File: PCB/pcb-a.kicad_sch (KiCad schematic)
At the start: 20 parts, among them Q3 BC337, Q4 BC337, SW1 config, U1 MCP23008-xP, U4 ATmega16L-8P, Y1 8Mhz

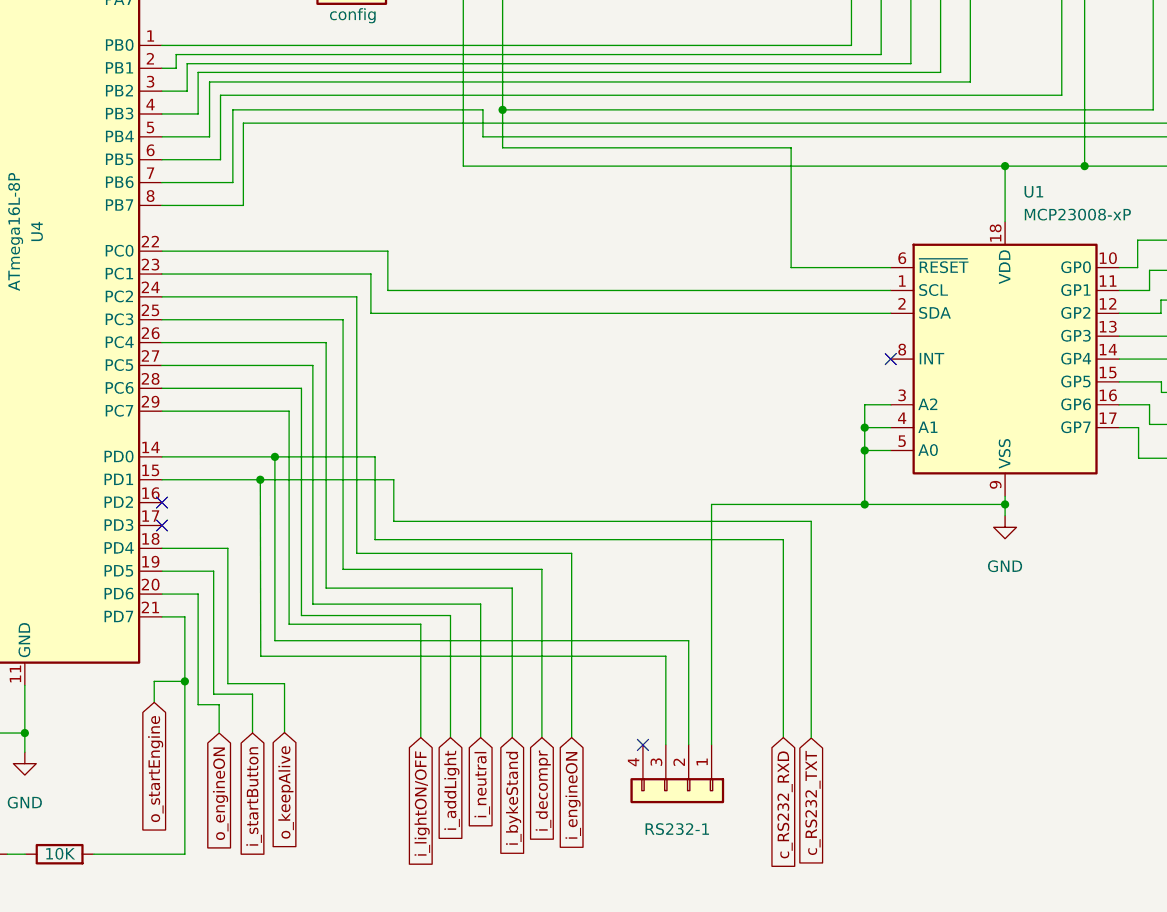
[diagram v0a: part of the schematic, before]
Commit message: Enhancement: RS232 port
RS232 4-wire connector is compatible with MAX232 driver module
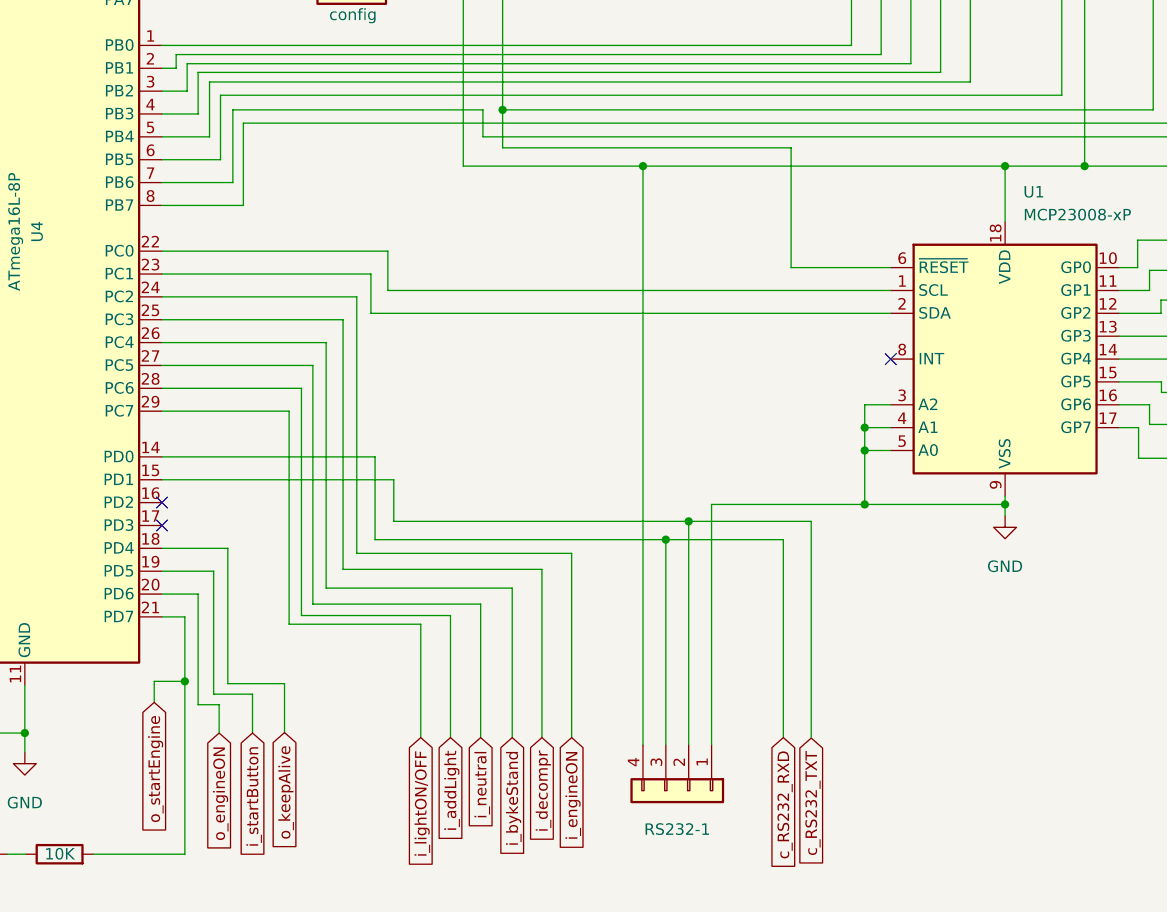
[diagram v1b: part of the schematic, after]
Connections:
- net c_RS232_RXD: now also RS232-1.3 (Pin_3); no longer RS232-1.2 (Pin_2)
- net c_RS232_TXT: now also RS232-1.2 (Pin_2); no longer RS232-1.3 (Pin_3)
- net tempPower: now also RS232-1.4 (Pin_4)
- no-connect marks 9 -> 8
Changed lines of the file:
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@@
   )
   (bus_alias "port-b" (members "PB0" "PB1" "PB2" "PB3" "PB4" "PB5" "PB6" "PB7"))
-  (junction (at 85.2424 121.158) (diameter 0) (color 0 0 0 0)
-  )
   (junction (at 59.0804 35.306) (diameter 0) (color 0 0 0 0)
   )
@@
   (junction (at 59.0804 149.3012) (diameter 0) (color 0 0 0 0)
   )
+  (junction (at 127.762 86.3092) (diameter 0) (color 0 0 0 0)
+  )
   (junction (at 40.8432 35.306) (diameter 0) (color 0 0 0 0)
   )
@@
   (junction (at 40.8432 45.8724) (diameter 0) (color 0 0 0 0)
   )
-  (junction (at 86.868 118.618) (diameter 0) (color 0 0 0 0)
-  )
   (junction (at 152.4 123.9012) (diameter 0) (color 0 0 0 0)
   )
@@
   (junction (at 176.8348 86.3092) (diameter 0) (color 0 0 0 0)
   )
+  (junction (at 130.302 127.8128) (diameter 0) (color 0 0 0 0)
+  )
   (junction (at 152.4 115.3668) (diameter 0) (color 0 0 0 0)
   )
@@
   )
   (junction (at 36.8808 62.738) (diameter 0) (color 0 0 0 0)
+  )
+  (junction (at 132.842 125.7808) (diameter 0) (color 0 0 0 0)
   )
   (junction (at 33.9852 86.8172) (diameter 0) (color 0 0 0 0)
@@
   (no_connect (at 74.3204 62.738))
   (no_connect (at 186.9948 49.4792))
-  (no_connect (at 127.762 150.622))
   (no_connect (at 61.6204 42.418))
   (no_connect (at 74.3204 60.198))
@@
     (stroke (width 0) (type default) (color 0 0 0 0))
   )
-  (wire (pts (xy 74.3204 118.618) (xy 86.868 118.618))
+  (wire (pts (xy 74.3204 118.618) (xy 97.9932 118.618))
     (stroke (width 0) (type default) (color 0 0 0 0))
   )
@@
     (stroke (width 0) (type default) (color 0 0 0 0))
   )
-  (wire (pts (xy 132.842 139.0396) (xy 86.868 139.0396))
-    (stroke (width 0) (type default) (color 0 0 0 0))
-  )
   (wire (pts (xy 74.3204 52.578) (xy 93.1164 52.578))
     (stroke (width 0) (type default) (color 0 0 0 0))
   )
+  (wire (pts (xy 127.762 86.3092) (xy 107.7976 86.3092))
+    (stroke (width 0) (type default) (color 0 0 0 0))
+  )
   (wire (pts (xy 74.3204 95.758) (xy 99.4156 95.758))
     (stroke (width 0) (type default) (color 0 0 0 0))
@@
     (stroke (width 0) (type default) (color 0 0 0 0))
   )
-  (wire (pts (xy 130.302 140.7668) (xy 130.302 150.622))
+  (wire (pts (xy 130.302 127.8128) (xy 130.302 150.622))
     (stroke (width 0) (type default) (color 0 0 0 0))
   )
@@
     (stroke (width 0) (type default) (color 0 0 0 0))
   )
-  (wire (pts (xy 97.9932 127.8128) (xy 143.3576 127.8128))
+  (wire (pts (xy 97.9932 127.8128) (xy 130.302 127.8128))
     (stroke (width 0) (type default) (color 0 0 0 0))
   )
@@
     (stroke (width 0) (type default) (color 0 0 0 0))
   )
-  (wire (pts (xy 132.842 139.0396) (xy 132.842 150.622))
+  (wire (pts (xy 132.842 125.7808) (xy 132.842 150.622))
     (stroke (width 0) (type default) (color 0 0 0 0))
   )
@@
     (stroke (width 0) (type default) (color 0 0 0 0))
   )
+  (wire (pts (xy 132.842 125.7808) (xy 146.4564 125.7808))
+    (stroke (width 0) (type default) (color 0 0 0 0))
+  )
   (wire (pts (xy 184.0484 115.0112) (xy 184.0484 112.8268))
     (stroke (width 0) (type default) (color 0 0 0 0))
@@
     (stroke (width 0) (type default) (color 0 0 0 0))
   )
-  (wire (pts (xy 100.076 125.7808) (xy 146.4564 125.7808))
+  (wire (pts (xy 100.076 125.7808) (xy 132.842 125.7808))
     (stroke (width 0) (type default) (color 0 0 0 0))
   )
@@
     (stroke (width 0) (type default) (color 0 0 0 0))
   )
-  (wire (pts (xy 74.3204 121.158) (xy 85.2424 121.158))
-    (stroke (width 0) (type default) (color 0 0 0 0))
-  )
-  (wire (pts (xy 85.2932 140.7668) (xy 130.302 140.7668))
-    (stroke (width 0) (type default) (color 0 0 0 0))
-  )
   (wire (pts (xy 40.8432 50.038) (xy 43.8404 50.038))
     (stroke (width 0) (type default) (color 0 0 0 0))
   )
-  (wire (pts (xy 86.868 118.618) (xy 97.9932 118.618))
+  (wire (pts (xy 130.302 127.8128) (xy 143.3576 127.8128))
     (stroke (width 0) (type default) (color 0 0 0 0))
   )
@@
     (stroke (width 0) (type default) (color 0 0 0 0))
   )
-  (wire (pts (xy 85.2932 140.7668) (xy 85.2424 121.158))
-    (stroke (width 0) (type default) (color 0 0 0 0))
-  )
   (wire (pts (xy 152.4 123.9012) (xy 167.9956 123.9012))
     (stroke (width 0) (type default) (color 0 0 0 0))
@@
     (stroke (width 0) (type default) (color 0 0 0 0))
   )
+  (wire (pts (xy 127.762 86.3092) (xy 127.762 150.622))
+    (stroke (width 0) (type default) (color 0 0 0 0))
+  )
   (wire (pts (xy 155.2956 97.5868) (xy 144.2212 97.5868))
     (stroke (width 0) (type default) (color 0 0 0 0))
@@
     (stroke (width 0) (type default) (color 0 0 0 0))
   )
-  (wire (pts (xy 85.2424 121.158) (xy 100.076 121.158))
+  (wire (pts (xy 74.3204 121.158) (xy 100.076 121.158))
     (stroke (width 0) (type default) (color 0 0 0 0))
   )
@@
     (stroke (width 0) (type default) (color 0 0 0 0))
   )
-  (wire (pts (xy 167.9956 86.3092) (xy 107.7976 86.3092))
+  (wire (pts (xy 167.9956 86.3092) (xy 127.762 86.3092))
     (stroke (width 0) (type default) (color 0 0 0 0))
   )
@@
     (stroke (width 0) (type default) (color 0 0 0 0))
   )
-  (wire (pts (xy 86.868 118.618) (xy 86.868 139.0396))
-    (stroke (width 0) (type default) (color 0 0 0 0))
-  )

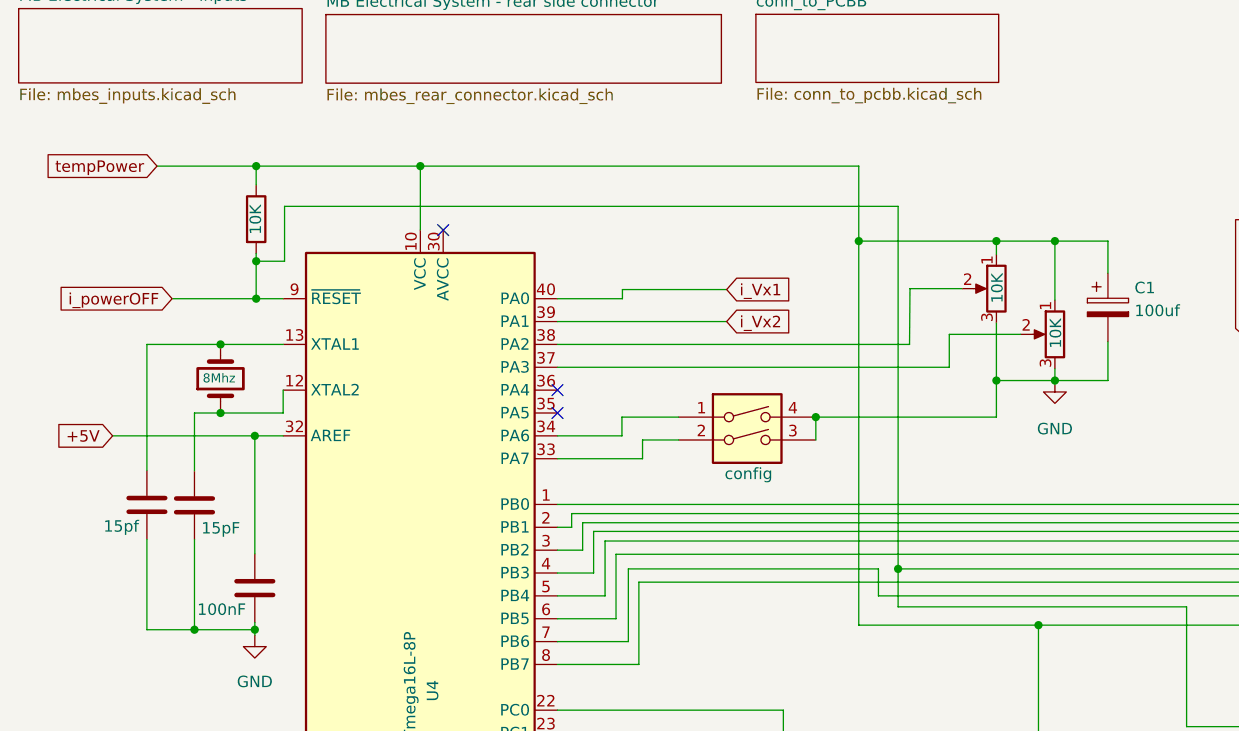
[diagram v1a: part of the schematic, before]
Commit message: Fixes for analog inputs
- ground reference missed
- AVCC was not connected
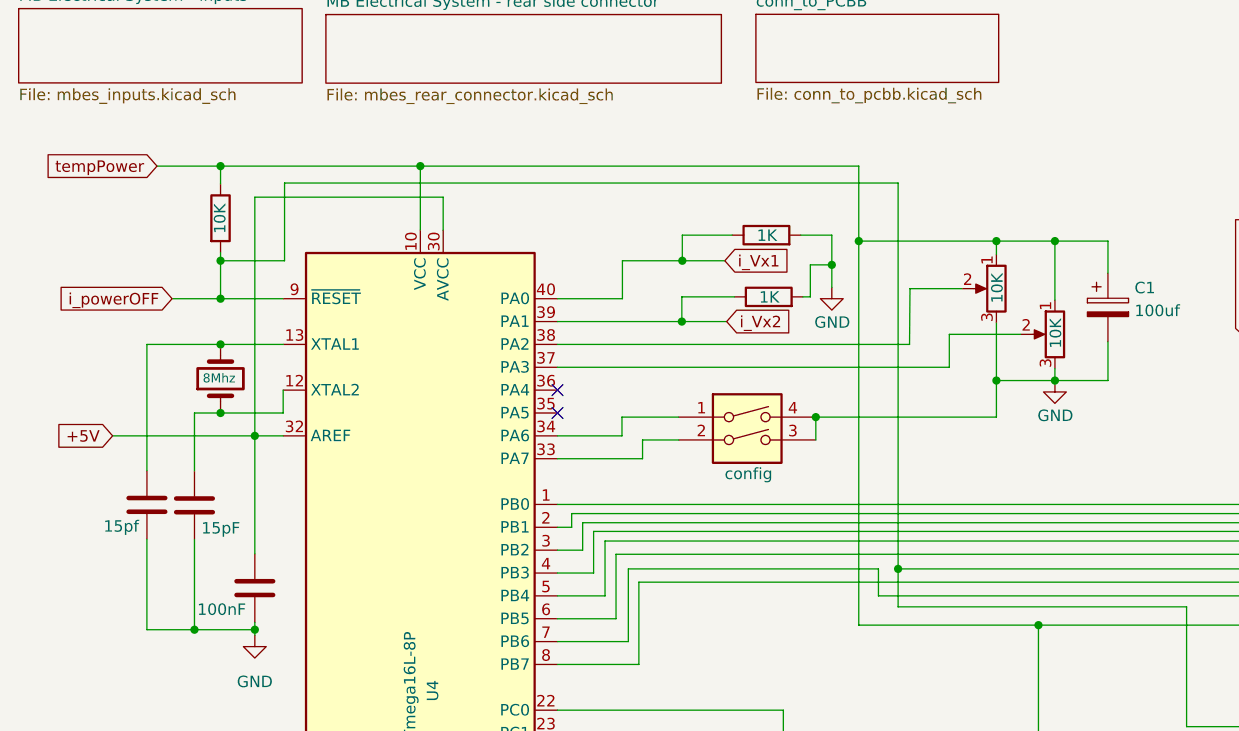
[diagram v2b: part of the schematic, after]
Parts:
- added R3, R4: 1K, Resistor_THT:R_Axial_DIN0207_L6.3mm_D2.5mm_P7.62mm_Horizontal, symbol Device:R
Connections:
- net +5V: now also U4.30 (AVCC)
- net GND: now also R3.2, R4.2
- net i_Vx1: now also R3.1
- net i_Vx2: now also R4.1
- no-connect marks 8 -> 7

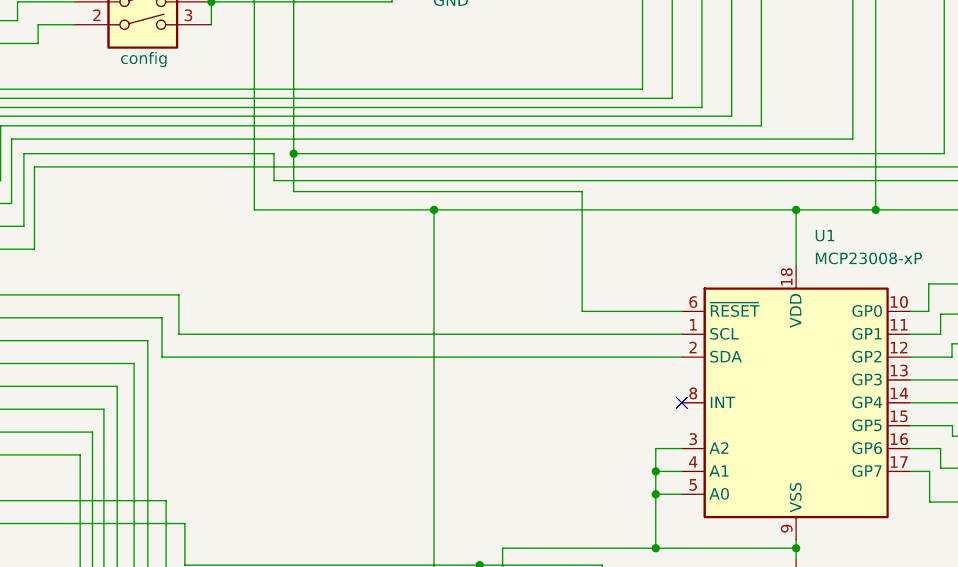
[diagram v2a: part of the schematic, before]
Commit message: Pull-up resistors missing on I2C has been fixed
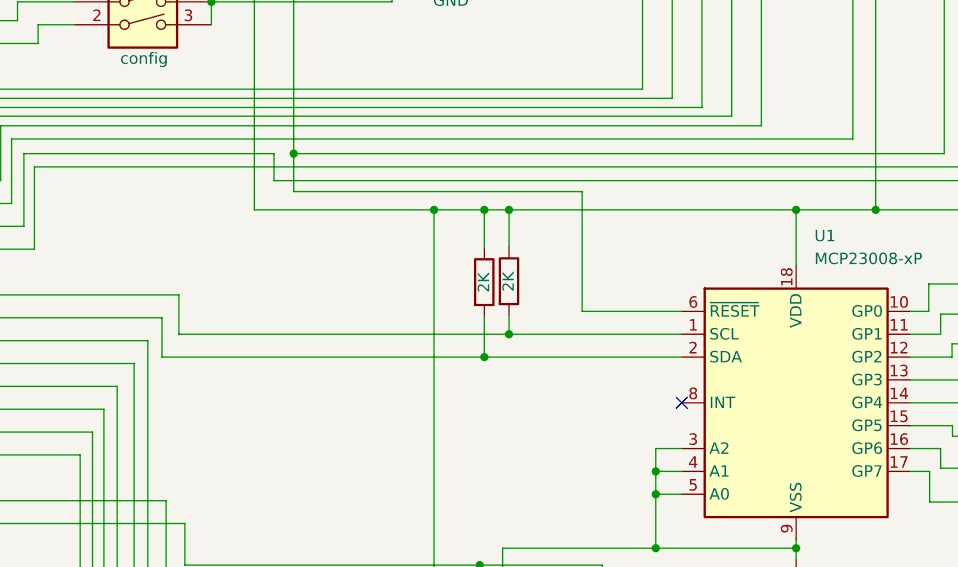
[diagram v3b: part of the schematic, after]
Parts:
- added R10, R5: 2K, Resistor_THT:R_Axial_DIN0207_L6.3mm_D2.5mm_P7.62mm_Horizontal, symbol Device:R
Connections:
- net tempPower: now also R10.1, R5.1
- net at U1.1 (SCL), U4.22 (PC0): now also R10.2
- net at U1.2 (SDA), U4.23 (PC1): now also R5.2
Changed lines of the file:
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@@
   (junction (at 88.1888 45.8216) (diameter 0) (color 0 0 0 0)
   )
+  (junction (at 133.35 102.6668) (diameter 0) (color 0 0 0 0)
+  )
   (junction (at 59.0804 149.3012) (diameter 0) (color 0 0 0 0)
   )
@@
   (junction (at 123.0884 43.6372) (diameter 0) (color 0 0 0 0)
   )
+  (junction (at 136.0932 100.1268) (diameter 0) (color 0 0 0 0)
+  )
   (junction (at 107.7976 43.6372) (diameter 0) (color 0 0 0 0)
   )
   (junction (at 88.138 52.578) (diameter 0) (color 0 0 0 0)
   )
+  (junction (at 133.35 86.3092) (diameter 0) (color 0 0 0 0)
+  )
   (junction (at 152.4 123.9012) (diameter 0) (color 0 0 0 0)
   )
@@
   )
   (junction (at 130.302 127.8128) (diameter 0) (color 0 0 0 0)
+  )
+  (junction (at 136.0932 86.3092) (diameter 0) (color 0 0 0 0)
   )
   (junction (at 152.4 115.3668) (diameter 0) (color 0 0 0 0)
@@
     (stroke (width 0) (type default) (color 0 0 0 0))
   )
+  (wire (pts (xy 136.0932 100.1268) (xy 155.2956 100.1268))
+    (stroke (width 0) (type default) (color 0 0 0 0))
+  )
   (wire (pts (xy 157.5308 74.93) (xy 157.5308 54.2036))
     (stroke (width 0) (type default) (color 0 0 0 0))
@@
     (stroke (width 0) (type default) (color 0 0 0 0))
   )
+  (wire (pts (xy 136.0932 86.3092) (xy 136.0932 90.424))
+    (stroke (width 0) (type default) (color 0 0 0 0))
+  )
   (wire (pts (xy 189.5348 71.4756) (xy 189.5348 81.534))
     (stroke (width 0) (type default) (color 0 0 0 0))
@@
     (stroke (width 0) (type default) (color 0 0 0 0))
   )
+  (wire (pts (xy 133.35 86.3092) (xy 127.762 86.3092))
+    (stroke (width 0) (type default) (color 0 0 0 0))
+  )
   (wire (pts (xy 80.0608 131.318) (xy 80.0608 144.9832))
     (stroke (width 0) (type default) (color 0 0 0 0))
@@
     (stroke (width 0) (type default) (color 0 0 0 0))
   )
+  (wire (pts (xy 133.35 102.6668) (xy 97.536 102.6668))
+    (stroke (width 0) (type default) (color 0 0 0 0))
+  )
   (wire (pts (xy 129.5908 57.8104) (xy 129.5908 59.1312))
     (stroke (width 0) (type default) (color 0 0 0 0))
@@
     (stroke (width 0) (type default) (color 0 0 0 0))
   )
+  (wire (pts (xy 99.4156 100.1268) (xy 136.0932 100.1268))
+    (stroke (width 0) (type default) (color 0 0 0 0))
+  )
   (wire (pts (xy 52.8828 168.5544) (xy 52.8828 178.054))
     (stroke (width 0) (type default) (color 0 0 0 0))
@@
     (stroke (width 0) (type default) (color 0 0 0 0))
   )
-  (wire (pts (xy 155.2956 102.6668) (xy 97.536 102.6668))
+  (wire (pts (xy 155.2956 102.6668) (xy 133.35 102.6668))
+    (stroke (width 0) (type default) (color 0 0 0 0))
+  )
+  (wire (pts (xy 136.0932 98.044) (xy 136.0932 100.1268))
     (stroke (width 0) (type default) (color 0 0 0 0))
   )
@@
     (stroke (width 0) (type default) (color 0 0 0 0))
   )
+  (wire (pts (xy 136.0932 86.3092) (xy 133.35 86.3092))
+    (stroke (width 0) (type default) (color 0 0 0 0))
+  )
   (wire (pts (xy 88.1888 42.9768) (xy 88.1888 45.8216))
     (stroke (width 0) (type default) (color 0 0 0 0))
@@
     (stroke (width 0) (type default) (color 0 0 0 0))
   )
+  (wire (pts (xy 133.35 98.1456) (xy 133.35 102.6668))
+    (stroke (width 0) (type default) (color 0 0 0 0))
+  )
   (wire (pts (xy 36.8808 62.738) (xy 43.8404 62.738))
     (stroke (width 0) (type default) (color 0 0 0 0))
@@
     (stroke (width 0) (type default) (color 0 0 0 0))
   )
-  (wire (pts (xy 155.2956 100.1268) (xy 99.4156 100.1268))
-    (stroke (width 0) (type default) (color 0 0 0 0))
-  )
   (wire (pts (xy 74.3204 121.158) (xy 100.076 121.158))
     (stroke (width 0) (type default) (color 0 0 0 0))
@@
     (stroke (width 0) (type default) (color 0 0 0 0))
   )
-  (wire (pts (xy 167.9956 86.3092) (xy 127.762 86.3092))
+  (wire (pts (xy 167.9956 86.3092) (xy 136.0932 86.3092))
     (stroke (width 0) (type default) (color 0 0 0 0))
   )
   (wire (pts (xy 129.5908 43.6372) (xy 129.5908 50.1904))
+    (stroke (width 0) (type default) (color 0 0 0 0))
+  )
+  (wire (pts (xy 133.35 86.3092) (xy 133.35 90.5256))
     (stroke (width 0) (type default) (color 0 0 0 0))
   )
@@
     )
     (property "Datasheet" "~" (id 3) (at 97.79 49.8348 0)
+      (effects (font (size 1.27 1.27)) hide)
+    )
+    (pin "1")
+    (pin "2")
+  )
+  (symbol (lib_id "Device:R") (at 133.35 94.3356 0) (unit 1)
+    (in_bom yes) (on_board yes)
+    (property "Reference" "R5" (id 0) (at 138.9888 94.3356 90)
+      (effects (font (size 1.27 1.27)) hide)
+    )
+    (property "Value" "2K" (id 1) (at 133.2992 94.3864 90))
+    (property "Footprint" "Resistor_THT:R_Axial_DIN0207_L6.3mm_D2.5mm_P7.62mm_Horizontal" (id 2) (at 131.572 94.3356 90)
+      (effects (font (size 1.27 1.27)) hide)
+    )
+    (property "Datasheet" "~" (id 3) (at 133.35 94.3356 0)
       (effects (font (size 1.27 1.27)) hide)
     )
@@
     (pin "2")
   )
+  (symbol (lib_id "Device:R") (at 136.0932 94.234 0) (unit 1)
+    (in_bom yes) (on_board yes)
+    (property "Reference" "R10" (id 0) (at 141.732 94.234 90)
+      (effects (font (size 1.27 1.27)) hide)
+    )
+    (property "Value" "2K" (id 1) (at 136.0424 94.2848 90))
+    (property "Footprint" "Resistor_THT:R_Axial_DIN0207_L6.3mm_D2.5mm_P7.62mm_Horizontal" (id 2) (at 134.3152 94.234 90)
+      (effects (font (size 1.27 1.27)) hide)
+    )
+    (property "Datasheet" "~" (id 3) (at 136.0932 94.234 0)
+      (effects (font (size 1.27 1.27)) hide)
+    )
+    (pin "1")
+    (pin "2")
+  )
   (symbol (lib_id "Transistor_BJT:BC337") (at 52.07 162.7632 180) (unit 1)
     (in_bom yes) (on_board yes)
@@
       (reference "R4") (unit 1) (value "1K") (footprint "Resistor_THT:R_Axial_DIN0207_L6.3mm_D2.5mm_P7.62mm_Horizontal")
     )
+    (path "/055b21e7-cffa-4f59-9539-0bca3db554c1"
+      (reference "R5") (unit 1) (value "2K") (footprint "Resistor_THT:R_Axial_DIN0207_L6.3mm_D2.5mm_P7.62mm_Horizontal")
+    )
     (path "/b1e0026b-e442-4e9d-9275-b07005f83053"
       (reference "R6") (unit 1) (value "100K") (footprint "Resistor_THT:R_Axial_DIN0207_L6.3mm_D2.5mm_P7.62mm_Horizontal")
@@
       (reference "R9") (unit 1) (value "5K") (footprint "Resistor_THT:R_Axial_DIN0207_L6.3mm_D2.5mm_P7.62mm_Horizontal")
     )
+    (path "/bbb25e40-262d-497b-b57b-82a229d73b48"
+      (reference "R10") (unit 1) (value "2K") (footprint "Resistor_THT:R_Axial_DIN0207_L6.3mm_D2.5mm_P7.62mm_Horizontal")
+    )
     (path "/c9774949-c461-4c76-91ad-3c30a5da3235"
